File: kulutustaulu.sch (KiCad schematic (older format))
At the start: 23 parts

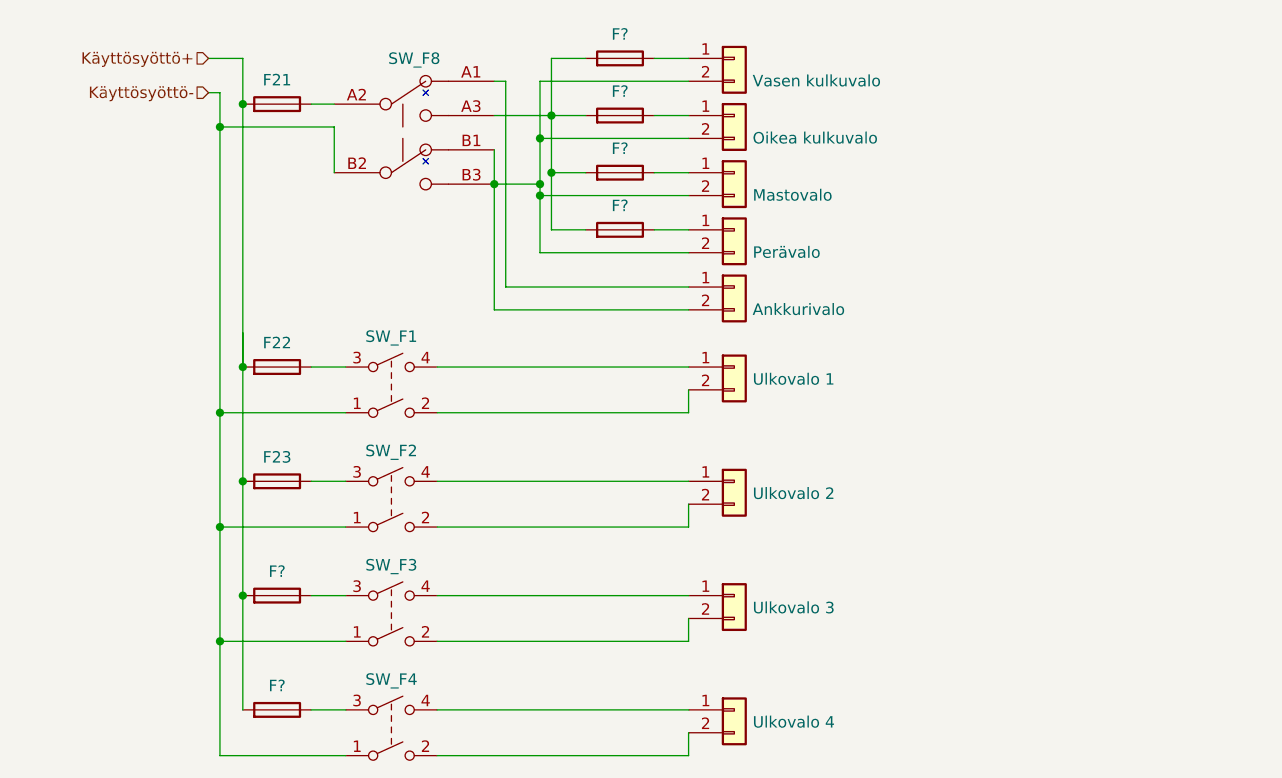
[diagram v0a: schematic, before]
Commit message: IDitä muutettu osoitteistusluonnoksen mukaan
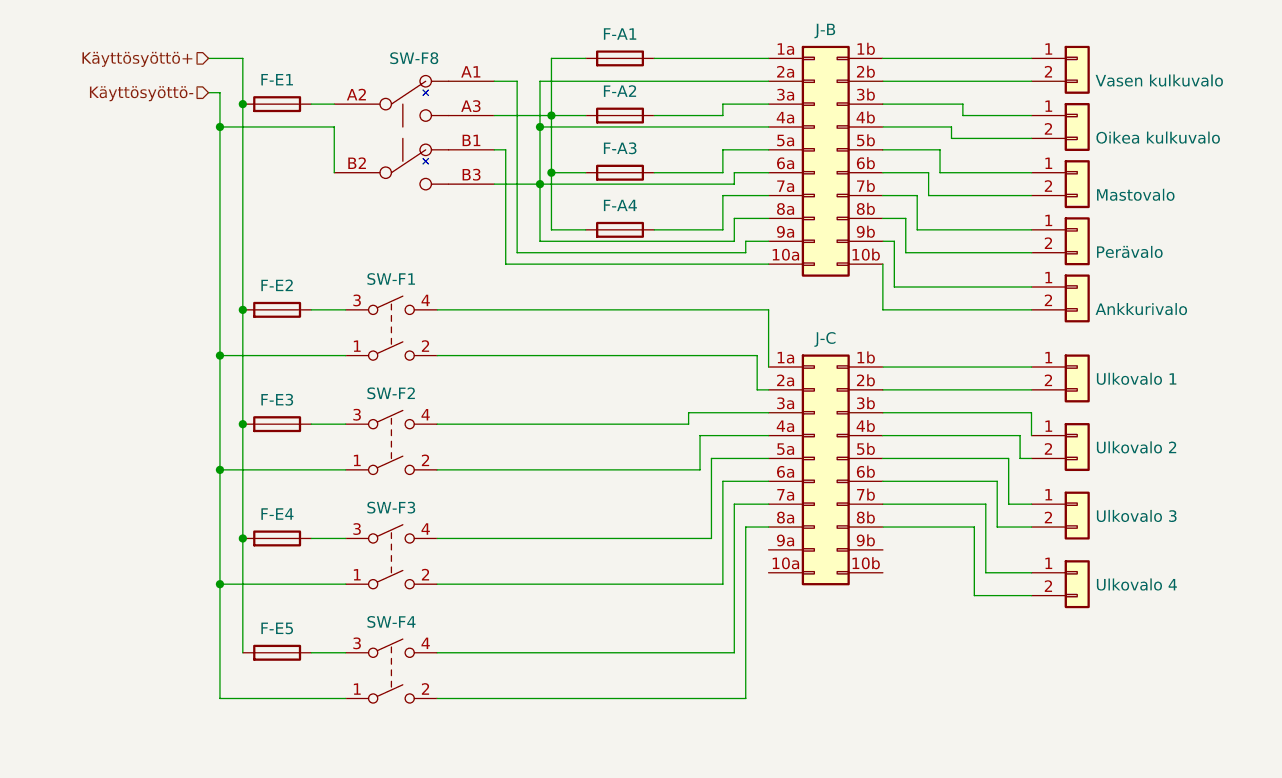
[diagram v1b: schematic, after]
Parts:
- added J-B, J-C: Conn_02x10_Row_Letter_Last, symbol Connector_Generic:Conn_02x10_Row_Letter_Last
- gave numbers to parts that had none: 6
- renumbered F21 to F-E1, F22 to F-E2, F23 to F-E3, SW_F1 to SW-F1, SW_F2 to SW-F2, SW_F3 to SW-F3, SW_F4 to SW-F4, SW_F8 to SW-F8
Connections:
- net at F-A2.1: now also J-B.3a (Pin_3a); no longer KulkuvaloSB.1 (Pin_1)
- net at F-A3.1: now also J-B.5a (Pin_5a); no longer Mastovalo.1 (Pin_1)
- net at F-A4.1: now also J-B.7a (Pin_7a); no longer Peravalo.1 (Pin_1)
- net at SW-F8.A1: now also J-B.9a (Pin_9a); no longer Ankkurivalo.1 (Pin_1)
- net at F-A1.1: now also J-B.1a (Pin_1a); no longer KulkuvaloBB.1 (Pin_1)
- net at SW-F1.2: now also J-C.2a (Pin_2a); no longer Ulkovalo1.2 (Pin_2)
- net at SW-F1.4: now also J-C.1a (Pin_1a); no longer Ulkovalo1.1 (Pin_1)
- net at SW-F2.2: now also J-C.4a (Pin_4a); no longer Ulkovalo2.2 (Pin_2)
- net at SW-F2.4: now also J-C.3a (Pin_3a); no longer Ulkovalo2.1 (Pin_1)
- net at SW-F3.2: now also J-C.6a (Pin_6a); no longer Ulkovalo3.2 (Pin_2)
- net at SW-F3.4: now also J-C.5a (Pin_5a); no longer Ulkovalo3.1 (Pin_1)
- net at SW-F4.2: now also J-C.8a (Pin_8a); no longer Ulkovalo4.2 (Pin_2)
- net at SW-F4.4: now also J-C.7a (Pin_7a); no longer Ulkovalo4.1 (Pin_1)
- new net: J-B.10a (Pin_10a), SW-F8.B1
- new net: Ankkurivalo.2 (Pin_2), J-B.10b (Pin_10b)
- new net: J-B.1b (Pin_1b), KulkuvaloBB.1 (Pin_1)
- new net: J-B.2a (Pin_2a), J-B.4a (Pin_4a), J-B.6a (Pin_6a), J-B.8a (Pin_8a), SW-F8.B3
- new net: J-B.2b (Pin_2b), KulkuvaloBB.2 (Pin_2)
- new net: J-B.3b (Pin_3b), KulkuvaloSB.1 (Pin_1)
- new net: J-B.4b (Pin_4b), KulkuvaloSB.2 (Pin_2)
- new net: J-B.5b (Pin_5b), Mastovalo.1 (Pin_1)
- new net: J-B.6b (Pin_6b), Mastovalo.2 (Pin_2)
- new net: J-B.7b (Pin_7b), Peravalo.1 (Pin_1)
- new net: J-B.8b (Pin_8b), Peravalo.2 (Pin_2)
- new net: Ankkurivalo.1 (Pin_1), J-B.9b (Pin_9b)
- new net: J-C.1b (Pin_1b), Ulkovalo1.1 (Pin_1)
- new net: J-C.2b (Pin_2b), Ulkovalo1.2 (Pin_2)
- new net: J-C.3b (Pin_3b), Ulkovalo2.1 (Pin_1)
- new net: J-C.4b (Pin_4b), Ulkovalo2.2 (Pin_2)
- new net: J-C.5b (Pin_5b), Ulkovalo3.1 (Pin_1)
- new net: J-C.6b (Pin_6b), Ulkovalo3.2 (Pin_2)
- new net: J-C.7b (Pin_7b), Ulkovalo4.1 (Pin_1)
- new net: J-C.8b (Pin_8b), Ulkovalo4.2 (Pin_2)
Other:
- moved on the sheet: F-E2, F-E3, F-E4, F-E5, SW-F1, SW-F2, SW-F3, SW-F4
